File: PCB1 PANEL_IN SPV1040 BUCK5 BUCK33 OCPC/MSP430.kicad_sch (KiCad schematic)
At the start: 15 parts, among them U20 MSP430F5529IPN, Y1 32K, Y2 CSTCR4M00G53-R0

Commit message: Change in MSP sch
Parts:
- removed C41, C43, C44, C48: 1u0, Capacitor_SMD:C_0603_1608Metric, symbol Device:C_Small
- removed C42: 10u, Capacitor_SMD:CP_Elec_3x5.3, symbol Device:C_Polarized_Small
- removed C45, C46: 1u1, Capacitor_SMD:C_0603_1608Metric, symbol Device:C_Small
- removed C47, C49: 1u0, Capacitor_SMD:C_0402_1005Metric_Pad0.74x0.62mm_HandSolder, symbol Device:C_Small
- removed C50: 10u, Capacitor_SMD:CP_Elec_4x3.9, symbol Device:C_Polarized_Small
- removed R53: 10K, Resistor_SMD:R_0603_1608Metric, symbol Device:R_Small
- removed U20: MSP430F5529IPN, footprintMSP:MSP430F5529IPN, symbol 2023-03-28_15-31-46:MSP430F5529IPN
- removed Y1: 32K, Crystal:Crystal_AT310_D3.0mm_L10.0mm_Horizontal_1EP_style1, symbol Device:Crystal_GND2_Small
- removed Y2: CSTCR4M00G53-R0, CSTCR4M00G53-R0:OSC_CSTCR4M00G53-R0, symbol CSTCR4M00G53-R0:CSTCR4M00G53-R0
- added J1, J2: Conn_02x10_Counter_Clockwise, symbol Connector_Generic:Conn_02x10_Counter_Clockwise
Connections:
- net 3V3: now also J1.1 (Pin_1)
- net 5V: now also J1.20 (Pin_20)
- net GND: now also J1.19 (Pin_19), J2.20 (Pin_20)
- net P1-2: now also J2.6 (Pin_6)
- net P1-3: now also J2.5 (Pin_5)
- net P1-4: now also J2.4 (Pin_4)
- net P1-5: now also J2.3 (Pin_3)
- net P1-6: now also J1.5 (Pin_5)
- net P2-0: now also J2.19 (Pin_19)
- net P2-2: now also J2.18 (Pin_18)
- net P2-3: now also J2.12 (Pin_12)
- net P2-4: now also J2.2 (Pin_2)
- net P2-5: now also J2.1 (Pin_1)
- net P2-6: now also J2.13 (Pin_13)
- net P2-7: now also J1.8 (Pin_8)
- net P3-0: now also J2.15 (Pin_15)
- net P3-1: now also J2.14 (Pin_14)
- net P3-2: now also J1.7 (Pin_7)
- net P3-3: now also J1.4 (Pin_4)
- net P3-4: now also J1.3 (Pin_3)
- net P3-5: now also J1.11 (Pin_11)
- net P3-6: now also J1.12 (Pin_12)
- net P3-7: now also J2.9 (Pin_9)
- net P4-0: now also J2.8 (Pin_8)
- net P4-1: now also J1.10 (Pin_10)
- net P4-2: now also J1.9 (Pin_9)
- net P4-3: now also J2.7 (Pin_7)
- new net P6-0: J1.18 (Pin_18)
- new net P6-1: J1.17 (Pin_17)
- new net P6-2: J1.16 (Pin_16)
- new net P6-3: J1.15 (Pin_15)
- new net P6-4: J1.14 (Pin_14)
- new net P6-5: J1.2 (Pin_2)
- new net P6-6: J1.6 (Pin_6)
- new net P7-0: J1.13 (Pin_13)
- new net P7-4: J2.17 (Pin_17)
- new net P8-1: J2.11 (Pin_11)
- new net P8-2: J2.10 (Pin_10)
- new net RST: J2.16 (Pin_16)
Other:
- note added: "1. Any GPIO pin can be configured for CS in SPI. 2. Distance between 2 sets of headers - 48.21 mm / 38.35 mm"
- note added: "I2C_SCL"
- note added: "I2C_SDA"
- note added: "SPI_CLK_1"
- note added: "SPI_MISO_1"
- note added: "SPI_MOSI_1"

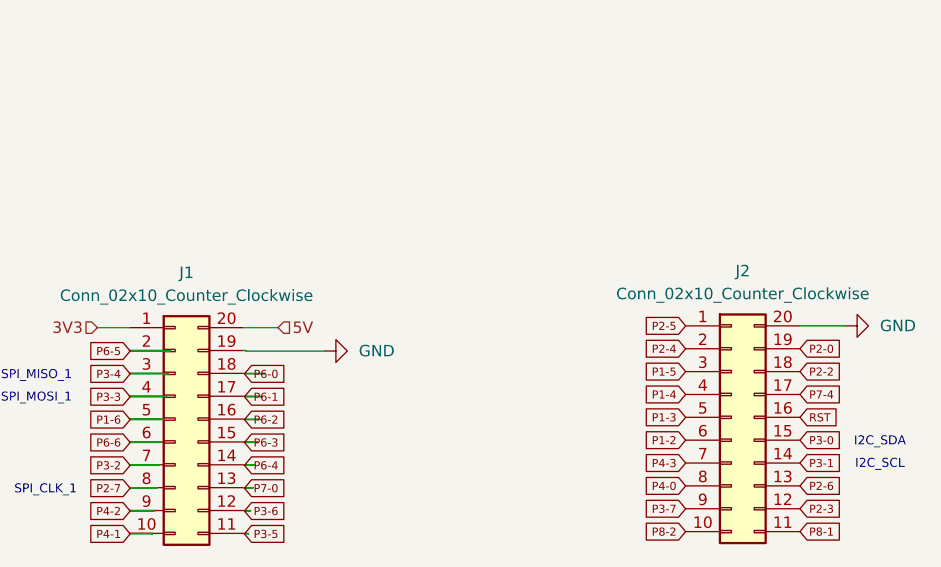
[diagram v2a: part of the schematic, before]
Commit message: Relabeling according to standards
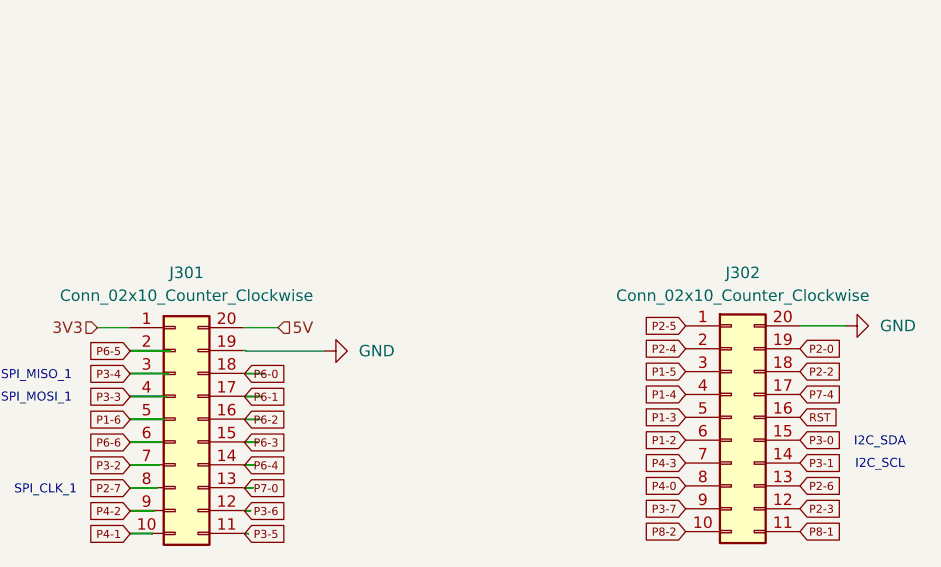
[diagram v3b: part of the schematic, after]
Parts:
- renumbered J1 to J301, J2 to J302
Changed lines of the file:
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@@
 		(dnp no)
 		(fields_autoplaced yes)
-		(property "Reference" "#PWR02"
+		(property "Reference" "#PWR0160"
 			(at 212.4256 78.2905 0)
 			(effects
@@
 		)
 		(instances
+			(project ""
+				(path "/494c9d9f-6b33-4248-a813-27ffaaa929bd/8d16167c-3e0d-4735-b524-3c01c883074e"
+					(reference "#PWR0160")
+					(unit 1)
+				)
+			)
 			(project "MSP430"
 				(path "/d440a0f9-62fd-4434-a9f7-19cfb6e06c06"
@@
 		(dnp no)
 		(fields_autoplaced yes)
-		(property "Reference" "J1"
+		(property "Reference" "J301"
 			(at 132.842 72.39 0)
 			(effects
@@
 		)
 		(instances
+			(project ""
+				(path "/494c9d9f-6b33-4248-a813-27ffaaa929bd/8d16167c-3e0d-4735-b524-3c01c883074e"
+					(reference "J301")
+					(unit 1)
+				)
+			)
 			(project "MSP430"
 				(path "/d440a0f9-62fd-4434-a9f7-19cfb6e06c06"
@@
 		(dnp no)
 		(fields_autoplaced yes)
-		(property "Reference" "J2"
-			(at 194.6456 72.1945 0)
+		(property "Reference" "J302"
+			(at 194.6456 72.39 0)
 			(effects
 				(font
@@
 		)
 		(property "Value" "Conn_02x10_Counter_Clockwise"
-			(at 194.6456 74.7345 0)
+			(at 194.6456 74.93 0)
 			(effects
 				(font
@@
 		)
 		(instances
+			(project ""
+				(path "/494c9d9f-6b33-4248-a813-27ffaaa929bd/8d16167c-3e0d-4735-b524-3c01c883074e"
+					(reference "J302")
+					(unit 1)
+				)
+			)
 			(project "MSP430"
 				(path "/d440a0f9-62fd-4434-a9f7-19cfb6e06c06"
@@
 		(dnp no)
 		(fields_autoplaced yes)
-		(property "Reference" "#PWR01"
+		(property "Reference" "#PWR0159"
 			(at 154.5136 81.0845 0)
 			(effects
@@
 		)
 		(instances
+			(project ""
+				(path "/494c9d9f-6b33-4248-a813-27ffaaa929bd/8d16167c-3e0d-4735-b524-3c01c883074e"
+					(reference "#PWR0159")
+					(unit 1)
+				)
+			)
 			(project "MSP430"
 				(path "/d440a0f9-62fd-4434-a9f7-19cfb6e06c06"
